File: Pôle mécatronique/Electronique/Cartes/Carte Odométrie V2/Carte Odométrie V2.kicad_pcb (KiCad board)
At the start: 2 copper layers, 72 x 86.2 mm, 14 parts, among them J1 Conn_01x08, J2 Conn_01x05, J3 Conn_01x04, J5 Conn_01x07, J6 Conn_01x04, U1 TCAN332

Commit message: Carte Bras test Résistance
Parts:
- moved BUS_CAN 3.63 mm to (189.6, 83.8), turned to 180 degrees
- renumbered J3 to BUS_CAN, J6 to CapteursTOF, J2 to LIDAR
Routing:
- net CAN_TX: track 102.6 -> 82.5 mm, vias 6 -> 2
- net +BATT: track 25.7 -> 7.25 mm, vias 2 -> 0
- net SPI_MISO: track 35.7 -> 38.4 mm
- net SPI_MOSI: track 34.8 -> 37.3 mm
- net SPI_CS: track 25.5 -> 26.5 mm
- net I2C_SDA: track 138.5 -> 137.8 mm
- net CAN_RX: track 172.3 -> 172.9 mm
- net CAN_L: track 22.4 -> 22.9 mm
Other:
- board text added: "+5V"

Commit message: MAJ carte actionneur
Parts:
- removed BUS_CAN: Conn_01x04, Connector_JST:JST_PH_B4B-PH-K_1x04_P2.00mm_Vertical
- added C1: C, Capacitor_SMD:C_1206_3216Metric, B.Cu at (199.8, 95.1)
- added C2: C, Capacitor_SMD:C_1206_3216Metric, B.Cu at (199.8, 97.9)
- added J4: Conn_01x04, Connector_JST:JST_PH_B4B-PH-K_1x04_P2.00mm_Vertical, F.Cu at (189.6, 83.8)
- added R3: R, Resistor_THT:R_Axial_DIN0207_L6.3mm_D2.5mm_P10.16mm_Horizontal, F.Cu at (192.1, 72.0)
- added TP1: TestPoint, TestPoint:TestPoint_Pad_D2.0mm, B.Cu at (187.0, 65.0)
- U1: value TCAN332 -> MCP2551-I-P; footprint empreinte:SO-8_S -> Package_DIP:DIP-8_W7.62mm; moved to F.Cu
- moved J1 11.3 mm to (154.6, 143.0)
- moved REF 8.33 mm to (132.0, 147.5)
- moved REF 7.99 mm to (200.0, 147.5)
- moved J6 6.92 mm to (158.5, 72.0), turned to 90 degrees
- moved U1 5.36 mm to (188.2, 100.8), turned to 90 degrees
- moved REF 4.97 mm to (201.0, 65.0)
- moved R2 4.13 mm to (152.8, 75.2)
- moved REF 4.11 mm to (132.0, 65.0)
- renumbered CapteursTOF to J6
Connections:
- A1 pad 4.1: +BATT -> unconnected-(A1-Pad4.1)
- U1 pad 1: CAN_RX -> CAN_TX
- U1 pad 3: +3V3 -> +5V
- U1 pad 4: CAN_TX -> CAN_RX
- U1 pad 8: unconnected-(U1-Pad8) -> GND
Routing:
- net +3V3: track 30.5 -> 0.00 mm, vias 2 -> 0
- net +5V: track 252.6 -> 227.2 mm, vias 6 -> 2
- net CAN_L: track 22.9 -> 34.5 mm
- net I2C_SDA: track 137.8 -> 129.8 mm
- net +BATT: track 7.25 -> 0.00 mm
- net I2C_SCL: track 136.3 -> 132.2 mm
- net CAN_H: track 20.6 -> 24.3 mm
- net CAN_TX: track 82.5 -> 79.5 mm
- net SPI_CLK: track 30.8 -> 29.5 mm
- net SPI_CS: track 26.5 -> 25.3 mm
- net CAN_RX: track 172.9 -> 171.7 mm, vias 4 -> 2
- added copper zone on F.Cu, net GND
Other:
- board size 72 x 86.2 mm -> 75 x 88.5 mm
- board text removed: "+5V"
- board text removed: "CAN_RX"
- board text removed: "CAN_TX"
- board text removed: "ROBOTECH NANCY"

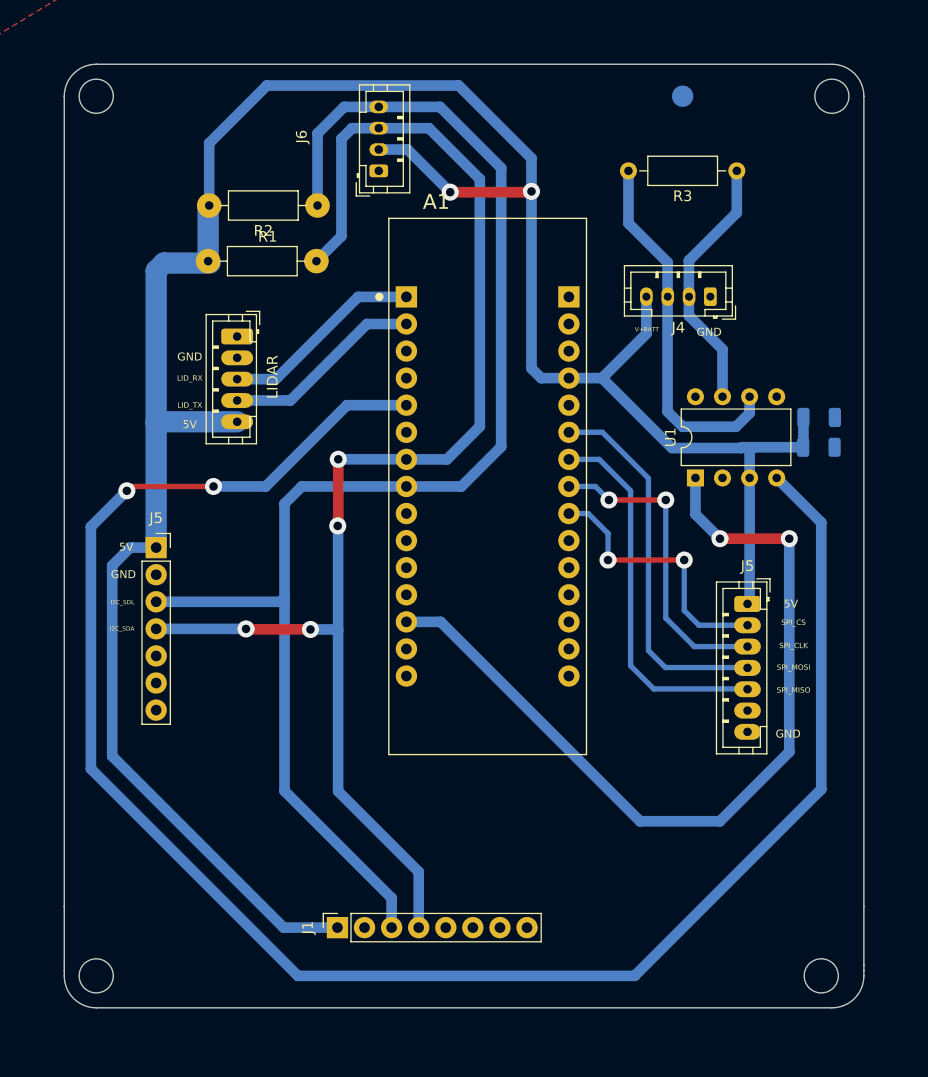
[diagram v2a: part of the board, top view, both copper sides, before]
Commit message: Sérigraphie Carte
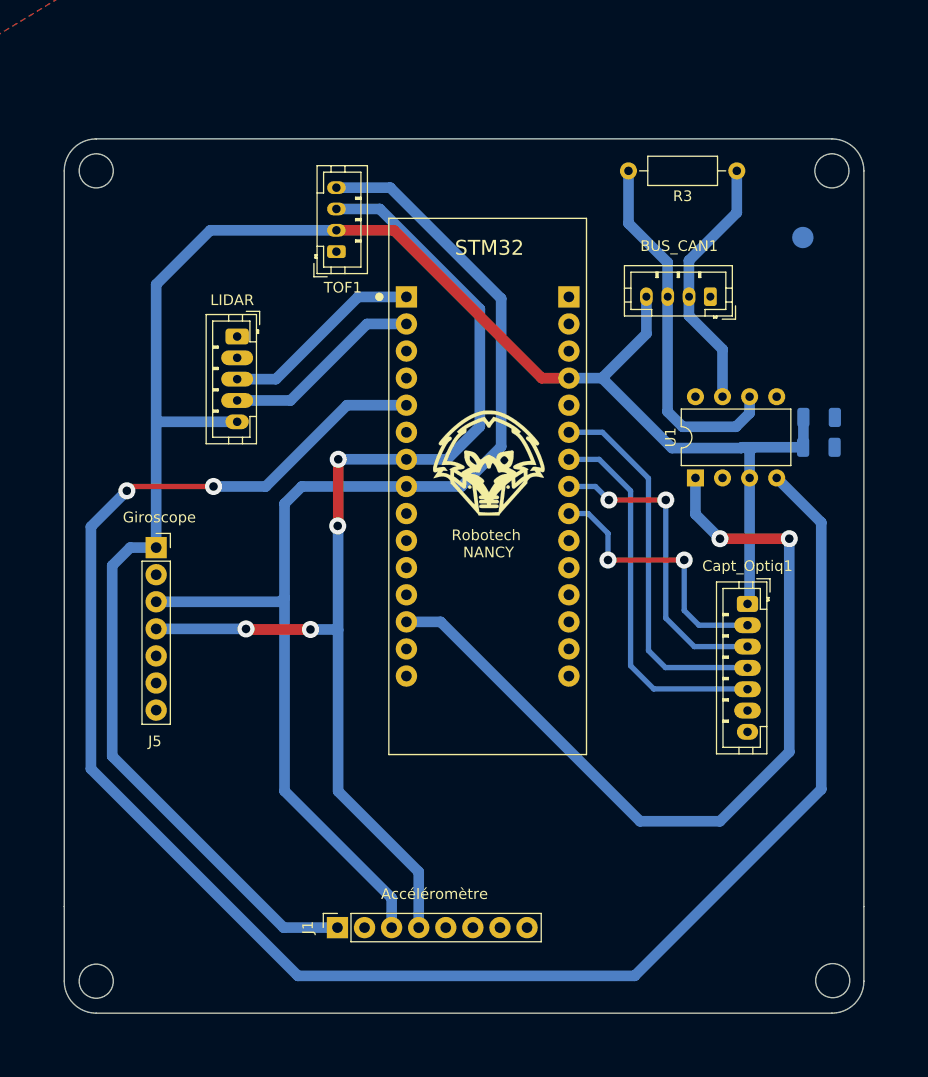
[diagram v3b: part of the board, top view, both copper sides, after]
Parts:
- removed R1, R2: 10000ohm, Resistor_THT:R_Axial_DIN0207_L6.3mm_D2.5mm_P10.16mm_Horizontal
- added G***: LOGO, Logos:logoRobotechNancy10x10, F.Cu at (168.8, 99.3)
- moved TP1 17.4 mm to (198.3, 78.2)
- moved TOF1 8.55 mm to (154.5, 79.6)
- moved REF 7.00 mm to (132.0, 72.0)
- moved REF 7.00 mm to (201.0, 72.0)
- moved REF 1.17 mm to (201.1, 147.9)
- moved REF 0.50 mm to (132.0, 148.0)
- renumbered J4 to BUS_CAN1, J5 to Capt_Optiq1, A1 to STM32, J6 to TOF1
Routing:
- net +5V: track 227.2 -> 180.9 mm, vias 2 -> 0
- net I2C_SDA: track 129.8 -> 107.1 mm
- net I2C_SCL: track 132.2 -> 112.3 mm
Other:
- board size 75 x 88.5 mm -> 75 x 82 mm
- board text added: "+5V"
- board text added: "Accéléromètre"
- board text added: "CAN_H"
- board text added: "CAN_L"
- board text added: "CAN_RX"
- board text added: "CAN_TX"
- board text added: "Giroscope"
- board text added: "I2C_SCL"
- board text added: "Robotech NANCY"
- board text added: "UART_RX"
- board text added: "UART_TX"
- board text removed: "V+BATT"

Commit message: maj final carte normalement
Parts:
- added +5V: TestPoint, TestPoint:TestPoint_Pad_D2.0mm, F.Cu at (198.2, 83.5)
- added C3: C, Capacitor_SMD:C_1206_3216Metric, B.Cu at (182.0, 90.0)
- added C4: C, Capacitor_SMD:C_1206_3216Metric, B.Cu at (179.5, 90.0)
- added CAN_H: TestPoint, TestPoint:TestPoint_Pad_D2.0mm, F.Cu at (188.5, 89.5)
- added CAN_L: TestPoint, TestPoint:TestPoint_Pad_D2.0mm, F.Cu at (195.5, 89.5)
- added I2C_SCL: TestPoint, TestPoint:TestPoint_Pad_D2.0mm, F.Cu at (132.6, 112.4)
- added I2C_SDA: TestPoint, TestPoint:TestPoint_Pad_D2.0mm, F.Cu at (132.8, 117.0)
- added LID_RX: TestPoint, TestPoint:TestPoint_Pad_D2.0mm, F.Cu at (133.7, 94.9)
- added LID_TX: TestPoint, TestPoint:TestPoint_Pad_D2.0mm, F.Cu at (133.8, 91.6)
- GND1: renamed from TP1; moved to F.Cu
- turned GND1 to 0 degrees
- renumbered STM32 to A1
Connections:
- A1 pad 4.15: ECHO7 -> unconnected-(A1-Pad4.15)
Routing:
- net +5V: track 180.9 -> 200.9 mm
- net UART1_RX: track 18.8 -> 31.0 mm
- net UART1_TX: track 19.1 -> 30.5 mm
- net I2C_SDA: track 107.1 -> 112.8 mm
- net I2C_SCL: track 112.3 -> 117.3 mm
- net CAN_H: track 24.3 -> 29.0 mm
- net CAN_L: track 34.5 -> 39.1 mm

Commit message: oui
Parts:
- added R1: R, Resistor_THT:R_Axial_DIN0207_L6.3mm_D2.5mm_P10.16mm_Horizontal, F.Cu at (172.4, 136.7)
- added R2: R, Resistor_THT:R_Axial_DIN0207_L6.3mm_D2.5mm_P10.16mm_Horizontal, F.Cu at (159.7, 136.7)
- renumbered +5V to +5V1, I2C_SCL to I2C_SCL1, I2C_SDA to I2C_SDA1, LID_RX to LID_RX1, LID_TX to LID_TX1, CAN_H to TP1, CAN_L to TP2
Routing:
- net +5V: track 200.9 -> 245.3 mm
- net CAN_RX: track 171.7 -> 173.0 mm
- net I2C_SCL: track 117.3 -> 116.8 mm

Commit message: carte odo
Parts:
- added Can_RX1: TestPoint, TestPoint:TestPoint_Pad_D2.0mm, B.Cu at (191.6, 138.4)
- added Can_TX1: TestPoint, TestPoint:TestPoint_Pad_D2.0mm, B.Cu at (186.2, 133.0)
- added SPI_CLK1: TestPoint, TestPoint:TestPoint_Pad_D2.0mm, B.Cu at (186.6, 115.4)
- added SPI_CS1: TestPoint, TestPoint:TestPoint_Pad_D2.0mm, B.Cu at (187.7, 111.5)
- added SPI_MISO1: TestPoint, TestPoint:TestPoint_Pad_D2.0mm, B.Cu at (181.5, 112.3)
- added SPI_MOSI1: TestPoint, TestPoint:TestPoint_Pad_D2.0mm, B.Cu at (184.6, 117.9)
- +5V1, GND1, I2C_SCL1, I2C_SDA1, LID_RX1, LID_TX1: moved to B.Cu
- Can_H1: renamed from TP1; moved to B.Cu
- Can_L1: renamed from TP2; moved to B.Cu
- moved I2C_SDA1 22.0 mm to (154.7, 118.7), turned to 180 degrees
- moved LID_TX1 21.9 mm to (154.8, 85.5), turned to 180 degrees
- moved LID_RX1 19.6 mm to (152.9, 90.9), turned to 180 degrees
- moved +5V1 19.4 mm to (184.3, 97.1), turned to 180 degrees
- moved Can_L1 18.5 mm to (181.9, 76.9), turned to 180 degrees
- moved Can_H1 13.7 mm to (191.7, 76.2), turned to 180 degrees
- moved I2C_SCL1 9.40 mm to (142.0, 112.5), turned to 180 degrees
- moved GND1 1.51 mm to (197.1, 79.2), turned to 180 degrees
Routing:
- net GND: track 0.00 -> 14.9 mm, vias 0 -> 4
- net UART1_RX: track 31.0 -> 18.8 mm
- net UART1_TX: track 30.5 -> 19.1 mm
- net +5V: track 245.3 -> 236.7 mm, vias 0 -> 2
- net I2C_SDA: track 112.8 -> 107.1 mm
- net I2C_SCL: track 116.8 -> 111.8 mm
- net CAN_H: track 29.0 -> 24.3 mm
- net CAN_L: track 39.1 -> 34.5 mm
- net SPI_MISO: track 38.4 -> 35.4 mm
- net SPI_MOSI: track 37.3 -> 35.5 mm
- removed copper zone on F.Cu, net GND

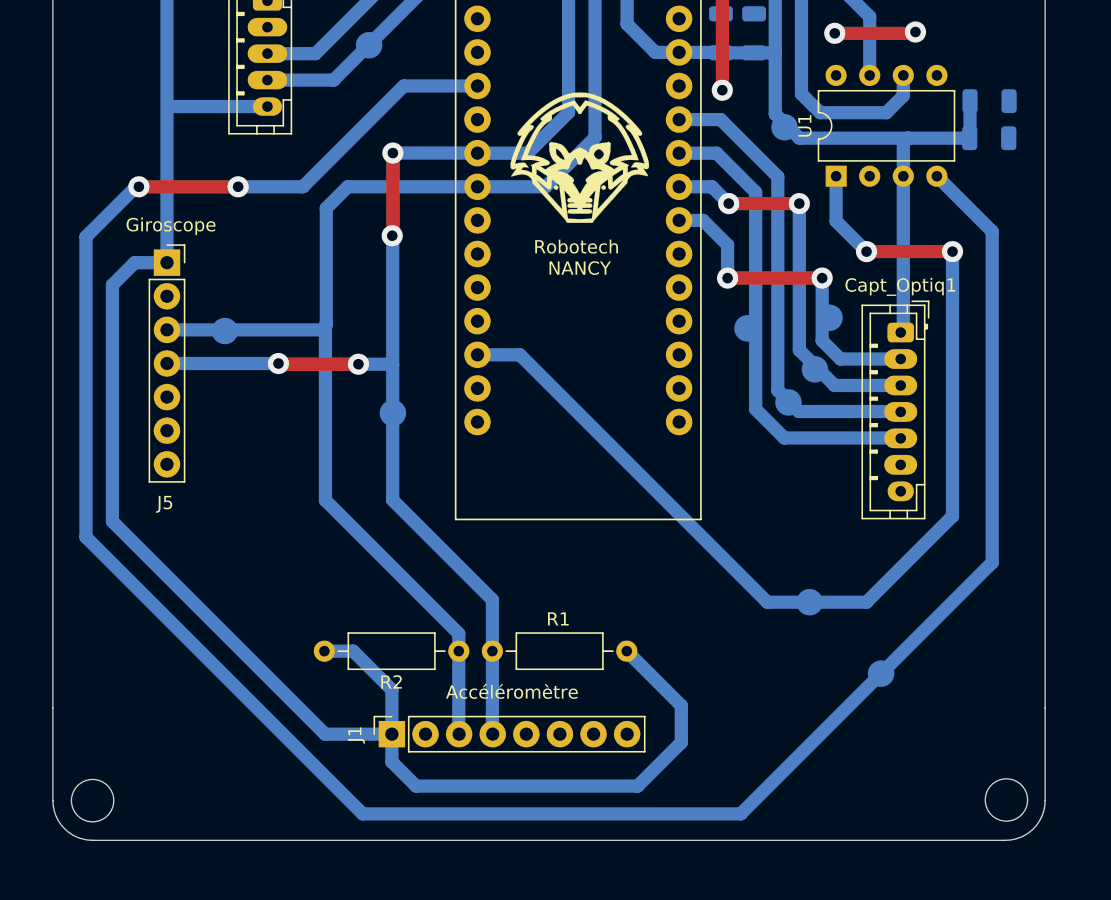
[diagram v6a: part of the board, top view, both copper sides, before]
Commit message: Xshut carte Odo
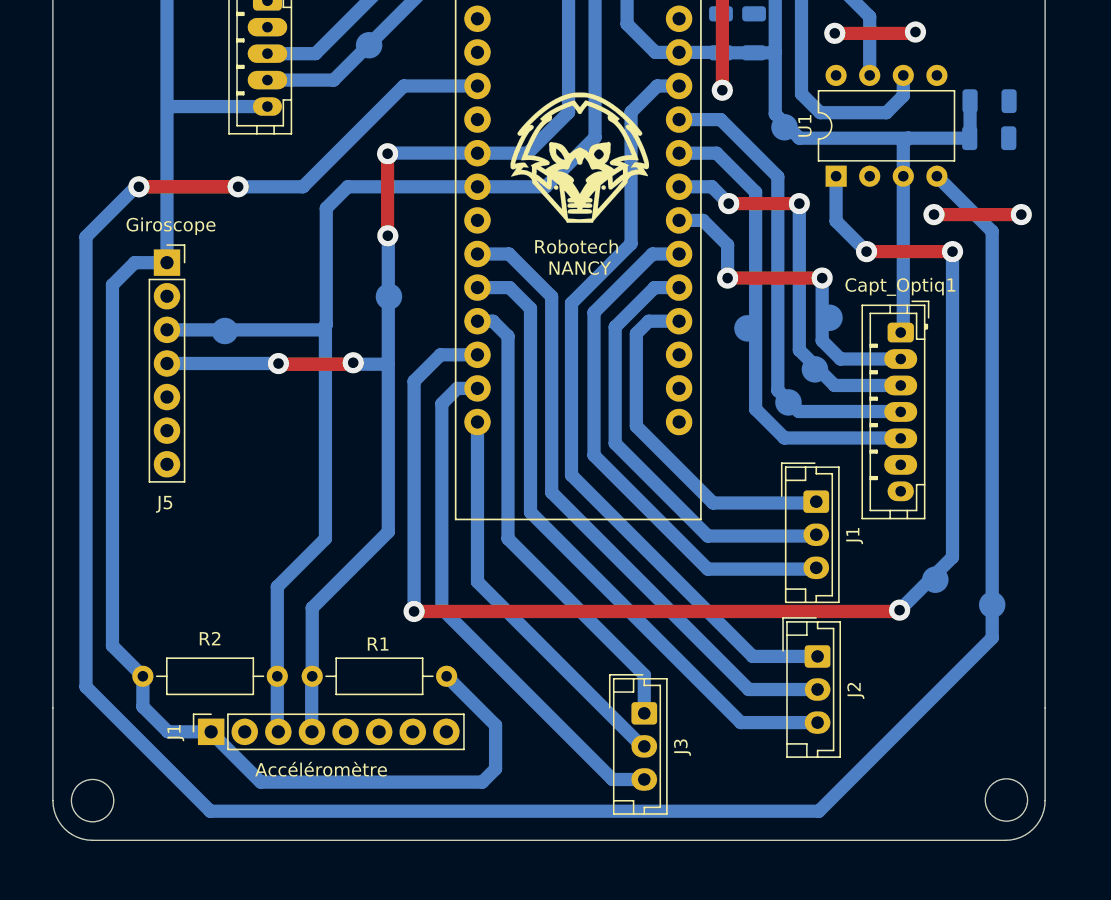
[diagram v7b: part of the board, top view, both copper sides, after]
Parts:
- added J1: Conn_01x03, Connector_JST:JST_EH_B3B-EH-A_1x03_P2.50mm_Vertical, F.Cu at (186.7, 125.4)
- added J2: Conn_01x03, Connector_JST:JST_EH_B3B-EH-A_1x03_P2.50mm_Vertical, F.Cu at (186.8, 137.1)
- added J3: Conn_01x03, Connector_JST:JST_EH_B3B-EH-A_1x03_P2.50mm_Vertical, F.Cu at (173.7, 141.4)
- moved R2 13.9 mm to (146.0, 138.6)
- moved R1 13.8 mm to (158.8, 138.6)
- moved J1 13.7 mm to (141.0, 142.8)
- moved Can_RX1 9.88 mm to (200.0, 133.2)
- moved Can_TX1 9.65 mm to (195.7, 131.3)
- moved I2C_SDA1 8.81 mm to (154.4, 109.9)
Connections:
- A1 pad 3.10: unconnected-(A1-Pad3.10) -> XShut5
- A1 pad 3.11: unconnected-(A1-Pad3.11) -> XShut6
- A1 pad 3.12: unconnected-(A1-Pad3.12) -> XShut7
- A1 pad 3.14: unconnected-(A1-Pad3.14) -> XShut9
- A1 pad 3.15: unconnected-(A1-Pad3.15) -> XShut8
- A1 pad 4.10: unconnected-(A1-Pad4.10) -> XShut3
- A1 pad 4.11: unconnected-(A1-Pad4.11) -> XShut2
- A1 pad 4.12: unconnected-(A1-Pad4.12) -> XShut1
- A1 pad 4.5: unconnected-(A1-Pad4.5) -> XShut4
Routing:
- net XShut4: track 0.00 -> 58.0 mm
- net XShut6: track 0.00 -> 48.3 mm
- net XShut5: track 0.00 -> 48.0 mm
- net XShut3: track 0.00 -> 39.7 mm
- net XShut9: track 0.00 -> 39.3 mm
- net XShut7: track 0.00 -> 35.5 mm
- net XShut2: track 0.00 -> 33.3 mm
- net XShut8: track 0.00 -> 29.8 mm
- net XShut1: track 0.00 -> 26.9 mm
- net CAN_TX: track 79.5 -> 101.7 mm, vias 2 -> 4
- net +5V: track 236.7 -> 217.4 mm
- net CAN_RX: track 173.0 -> 182.8 mm
- net GND: track 14.9 -> 21.5 mm, vias 4 -> 6
- net I2C_SCL: track 111.8 -> 108.9 mm
- net I2C_SDA: track 107.1 -> 106.1 mm

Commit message: crate
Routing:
- net XShut1: track 26.9 -> 25.9 mm
- net XShut8: track 29.8 -> 30.7 mm
- net XShut2: track 33.3 -> 32.6 mm
